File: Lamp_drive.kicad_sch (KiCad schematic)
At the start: 133 parts, among them J301 10146581-060_M, J302 T44007, J303 T44007, J304 10146581-060_M, J305 T44007, J306 T44007, Q301 MPF3N150, Q302 IXYH55N120, Q303 IXYH55N120, Q304 IXYH55N120, Q305 IXYH55N120, U301 IRS2184

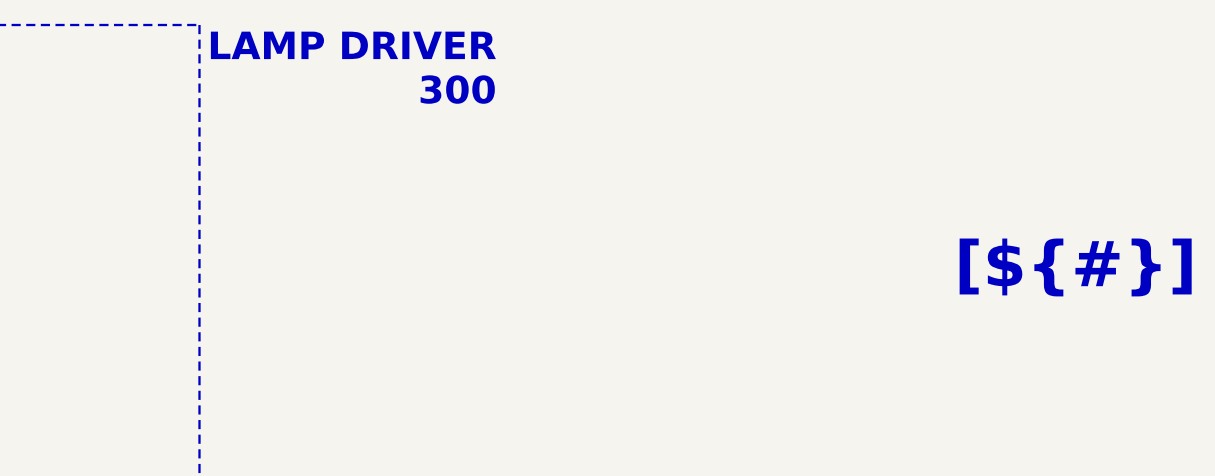
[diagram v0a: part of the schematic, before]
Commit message: Reworked sheet titles
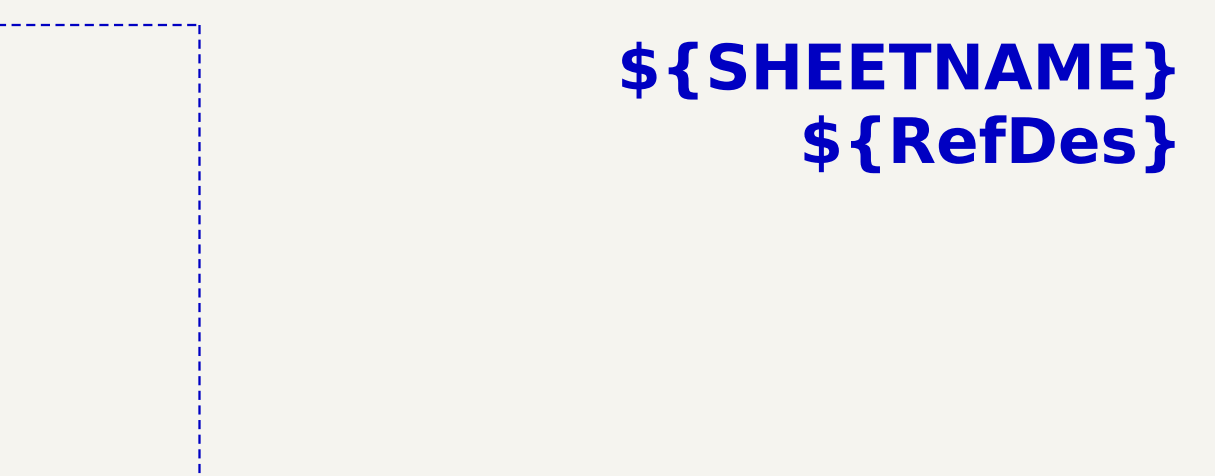
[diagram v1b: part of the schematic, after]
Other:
- note removed: "LAMP DRIVER 300"
- title: (none) -> ${SHEETNAME}
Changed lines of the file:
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@@
 	(paper "A3")
 	(title_block
+		(title "${SHEETNAME}")
 		(date "2025-01-12")
 	)
@@
 		)
 	)
-	(text "LAMP DRIVER\n300"
-		(exclude_from_sim no)
-		(at 325.12 19.05 0)
-		(effects
-			(font
-				(size 3.048 3.048)
-				(thickness 0.4064)
-				(bold yes)
-				(color 0 0 255 1)
-			)
-			(justify right)
-		)
-	)
 	(text "OFF-BOARD\nConnected through\nJ301"
 		(exclude_from_sim no)
@@
 		)
 	)
-	(text_box "[${#}] ${TITLE}"
+	(text_box "${SHEETNAME}\n${RefDes}"
 		(exclude_from_sim no)
-		(at 307.34 34.29 0)
-		(size 101.6 12.7)
-		(margins 5.9999 5.9999 5.9999 5.9999)
+		(at 342.9 15.24 0)
+		(size 60.96 15.24)
+		(margins 2.54 1.27 2.54 1.27)
 		(stroke
 			(width -0.0001)
